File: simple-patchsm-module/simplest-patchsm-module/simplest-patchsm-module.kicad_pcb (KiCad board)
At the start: 2 copper layers, 48 x 108 mm, 12 parts

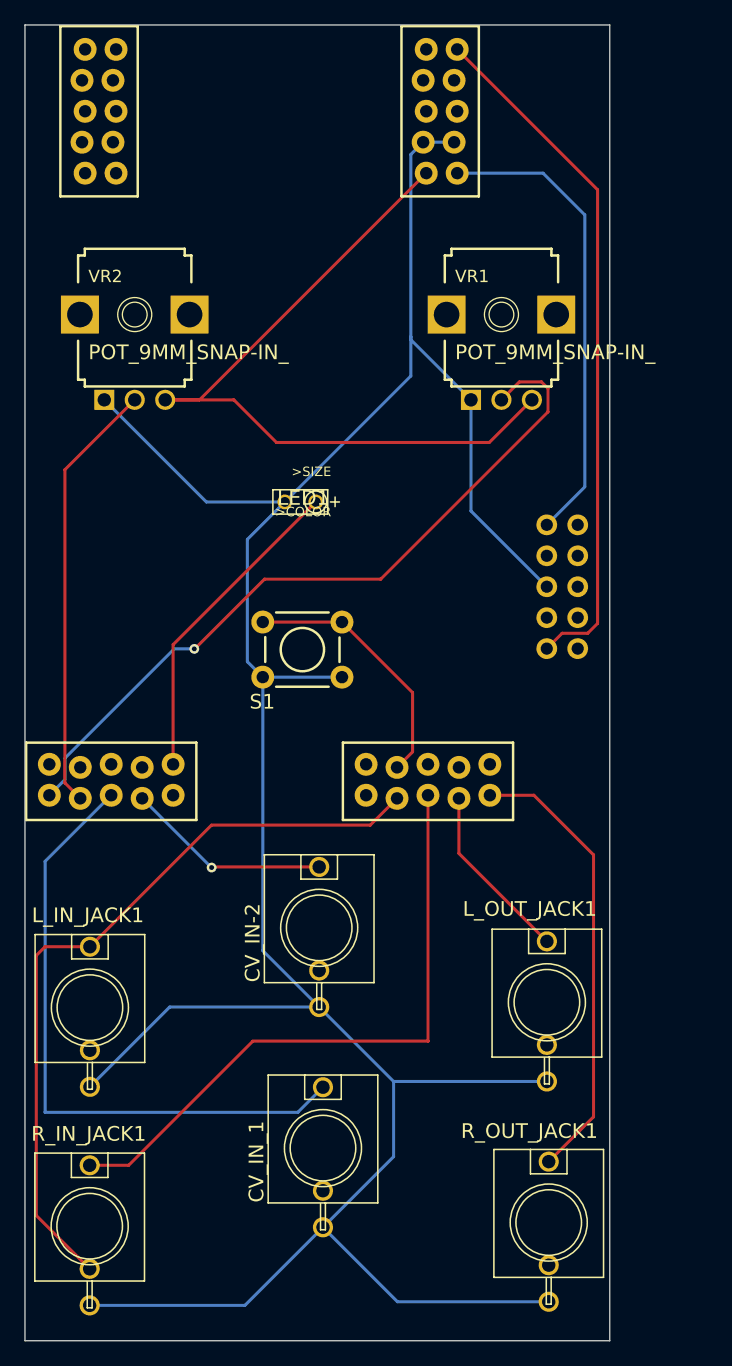
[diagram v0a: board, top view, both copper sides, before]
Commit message: Updates Patch SM boards to non-exploding footprint.
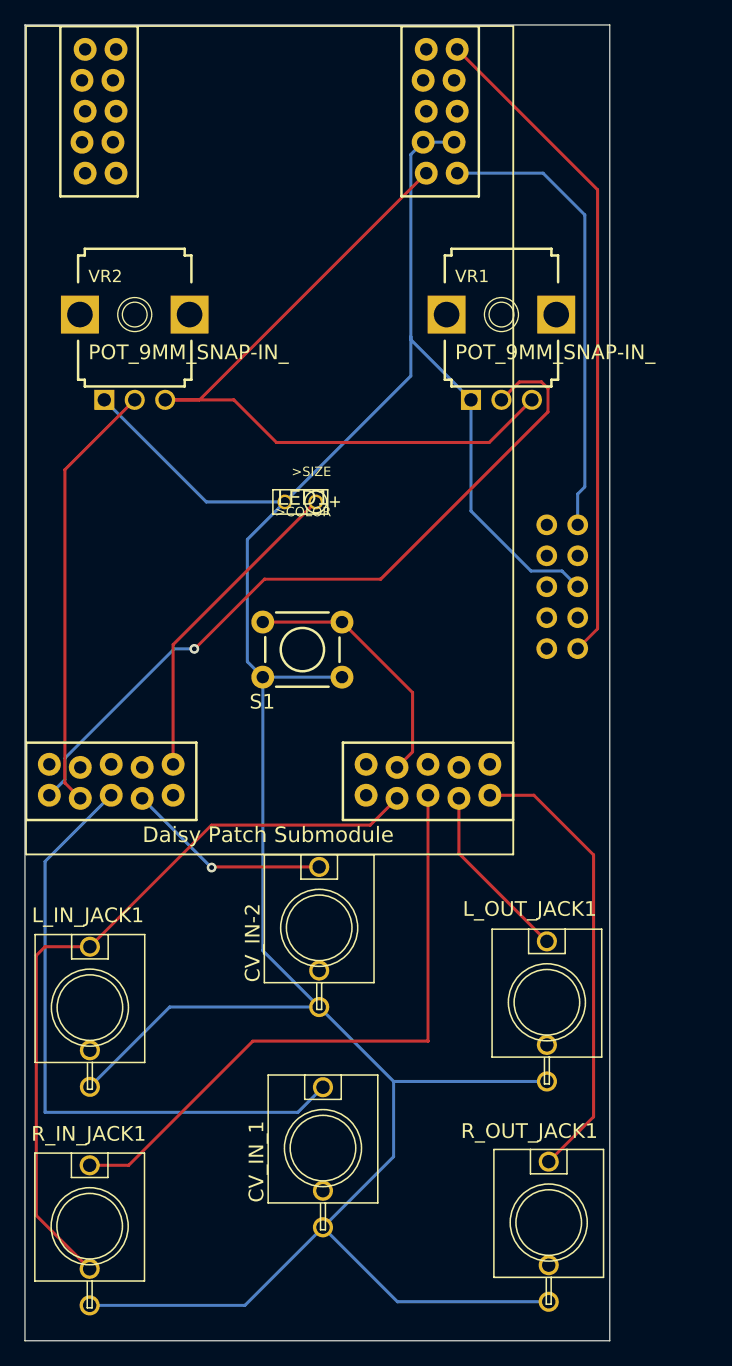
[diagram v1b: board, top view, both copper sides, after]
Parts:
- PATCH_SM1: value ES_DAISY_PATCH_SM_REV1 -> Daisy Patch Submodule; footprint ES_Daisy_Patch_SM_FB_Rev1:ES_DAISY_PATCH_SM_REV1 -> Lichen:Daisy_Patch_Submodule
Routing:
- net GND: track 231.9 -> 234.4 mm
- net -12V: track 56.9 -> 54.6 mm
- net +12V: track 38.6 -> 37.6 mm
